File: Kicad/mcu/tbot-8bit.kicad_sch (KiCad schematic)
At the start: 6 parts

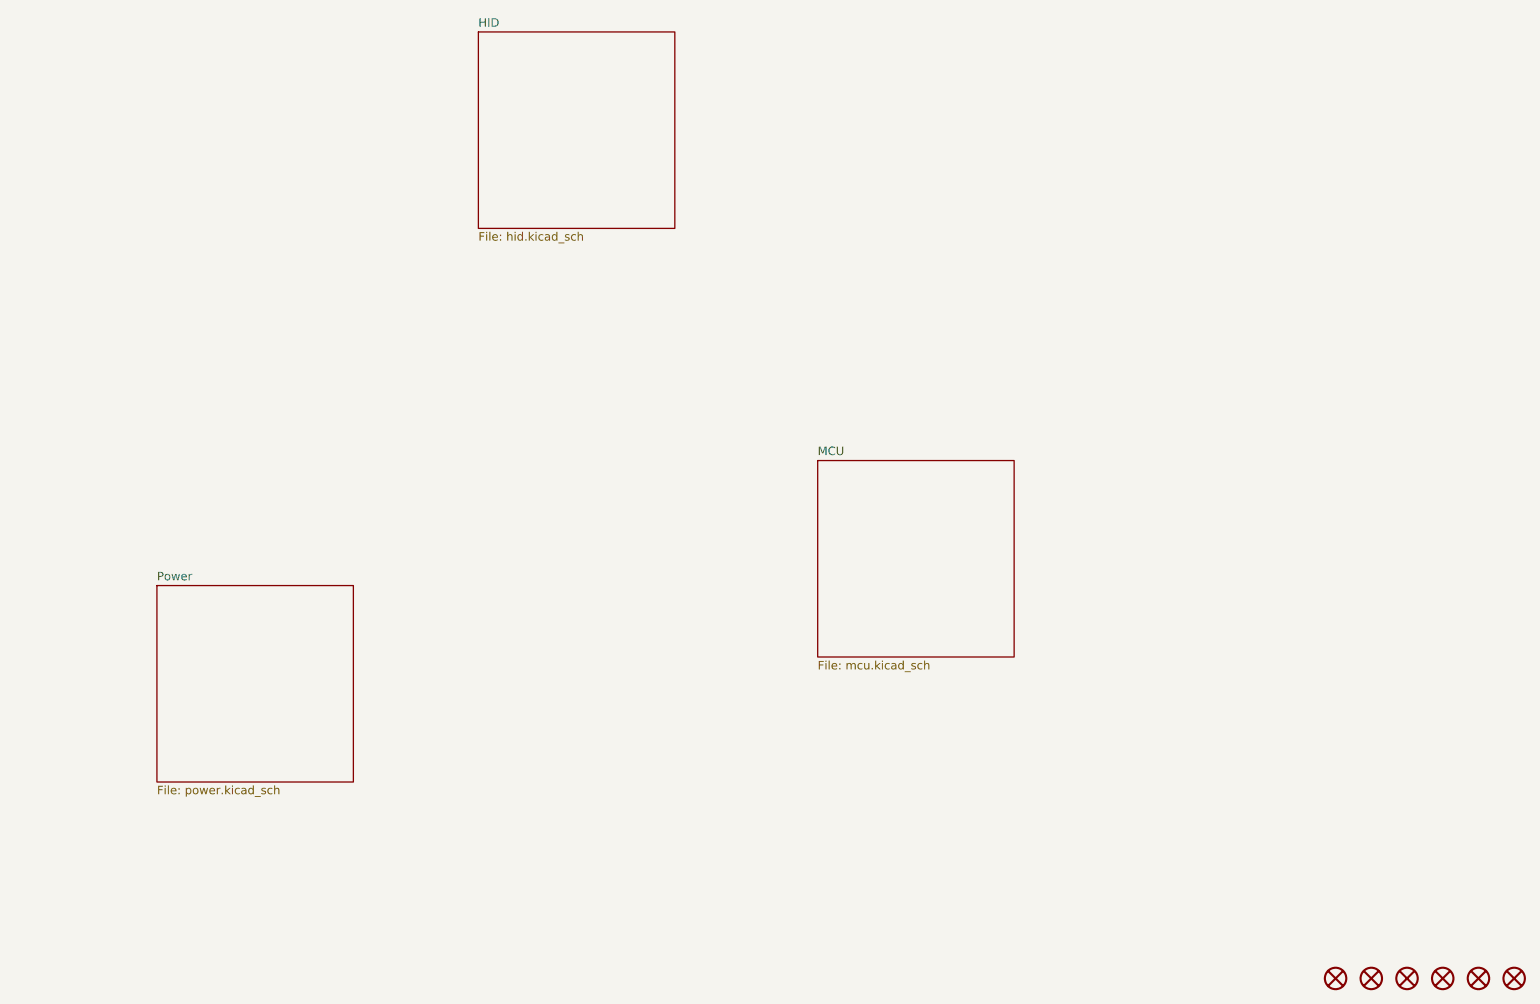
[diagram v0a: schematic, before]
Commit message: Update MCU 8Bit
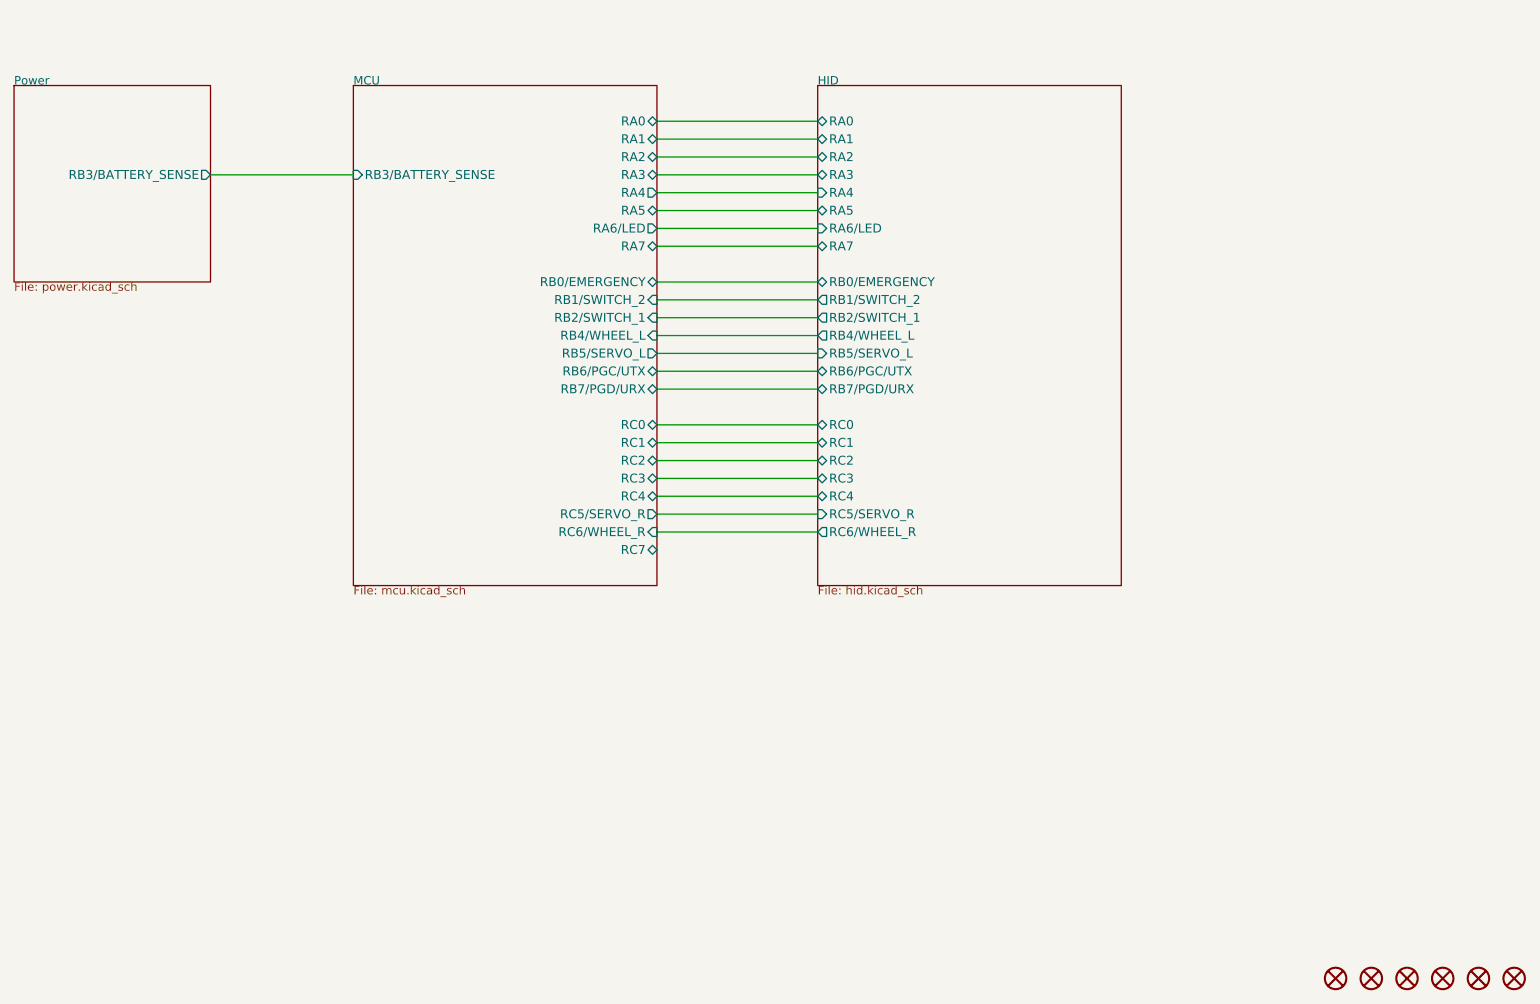
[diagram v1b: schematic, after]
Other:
- sheet HID ports: added RA0, RA1, RA2, RA3, RA4, RA5, RA6/LED, RA7, RB0/EMERGENCY, RB1/SWITCH_2, RB2/SWITCH_1, RB4/WHEEL_L, RB5/SERVO_L, RB6/PGC/UTX, RB7/PGD/URX, RC0, RC1, RC2, RC3, RC4, RC5/SERVO_R, RC6/WHEEL_R; removed none
- sheet MCU ports: added RA0, RA1, RA2, RA3, RA4, RA5, RA6/LED, RA7, RB0/EMERGENCY, RB1/SWITCH_2, RB2/SWITCH_1, RB3/BATTERY_SENSE, RB4/WHEEL_L, RB5/SERVO_L, RB6/PGC/UTX, RB7/PGD/URX, RC0, RC1, RC2, RC3, RC4, RC5/SERVO_R, RC6/WHEEL_R, RC7; removed none
- sheet Power ports: added RB3/BATTERY_SENSE; removed none

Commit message: Update MCU
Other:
- sheet HID ports: added none; removed RA7, RB1/SWITCH_2, RB2/SWITCH_1, RC3, RC4
- sheet MCU ports: added none; removed RA7, RB1/SWITCH_2, RB2/SWITCH_1, RC3, RC4, RC7

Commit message: Update MCU
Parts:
- added H107, H108: MOUNTING-HOLE-3MM, tronixio:M3, symbol tronixio:MOUNTING-HOLE-3MM
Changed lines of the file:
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@@
     (stroke (width 0) (type default) (color 0 0 0 0))
-  )
-  (symbol (lib_id "tronixio:MOUNTING-HOLE-MASK-3MM") (at 279.4 172.72 0) (unit 1)
-    (in_bom yes) (on_board yes)
-    (property "Reference" "H106" (id 0) (at 279.4 167.64 0)
-      (effects (font (size 1 1)) hide)
-    )
-    (property "Value" "MOUNTING-HOLE-MASK-3MM" (id 1) (at 279.4 170.18 0)
-      (effects (font (size 1 1)) hide)
-    )
-    (property "Footprint" "tronixio:M3-MASK" (id 2) (at 279.4 175.26 0)
-      (effects (font (size 1 1)) hide)
-    )
-    (property "Datasheet" "" (id 3) (at 279.4 172.72 0)
-      (effects (font (size 1 1)) hide)
-    )
-  )
-  (symbol (lib_id "tronixio:MOUNTING-HOLE-MASK-3MM") (at 274.32 172.72 0) (unit 1)
-    (in_bom yes) (on_board yes)
-    (property "Reference" "H105" (id 0) (at 274.32 167.64 0)
-      (effects (font (size 1 1)) hide)
-    )
-    (property "Value" "MOUNTING-HOLE-MASK-3MM" (id 1) (at 274.32 170.18 0)
-      (effects (font (size 1 1)) hide)
-    )
-    (property "Footprint" "tronixio:M3-MASK" (id 2) (at 274.32 175.26 0)
-      (effects (font (size 1 1)) hide)
-    )
-    (property "Datasheet" "" (id 3) (at 274.32 172.72 0)
-      (effects (font (size 1 1)) hide)
-    )
-  )
-  (symbol (lib_id "tronixio:MOUNTING-HOLE-MASK-3MM") (at 269.24 172.72 0) (unit 1)
-    (in_bom yes) (on_board yes)
-    (property "Reference" "H104" (id 0) (at 269.24 167.64 0)
-      (effects (font (size 1 1)) hide)
-    )
-    (property "Value" "MOUNTING-HOLE-MASK-3MM" (id 1) (at 269.24 170.18 0)
-      (effects (font (size 1 1)) hide)
-    )
-    (property "Footprint" "tronixio:M3-MASK" (id 2) (at 269.24 175.26 0)
-      (effects (font (size 1 1)) hide)
-    )
-    (property "Datasheet" "" (id 3) (at 269.24 172.72 0)
-      (effects (font (size 1 1)) hide)
-    )
   )
   (symbol (lib_id "tronixio:MOUNTING-HOLE-MASK-3MM") (at 264.16 172.72 0) (unit 1)
     (in_bom yes) (on_board yes)
-    (property "Reference" "H103" (id 0) (at 264.16 167.64 0)
+    (property "Reference" "H106" (id 0) (at 264.16 167.64 0)
       (effects (font (size 1 1)) hide)
     )
@@
     )
     (property "Datasheet" "" (id 3) (at 264.16 172.72 0)
+      (effects (font (size 1 1)) hide)
+    )
+  )
+  (symbol (lib_id "tronixio:MOUNTING-HOLE-MASK-3MM") (at 259.08 172.72 0) (unit 1)
+    (in_bom yes) (on_board yes)
+    (property "Reference" "H105" (id 0) (at 259.08 167.64 0)
+      (effects (font (size 1 1)) hide)
+    )
+    (property "Value" "MOUNTING-HOLE-MASK-3MM" (id 1) (at 259.08 170.18 0)
+      (effects (font (size 1 1)) hide)
+    )
+    (property "Footprint" "tronixio:M3-MASK" (id 2) (at 259.08 175.26 0)
+      (effects (font (size 1 1)) hide)
+    )
+    (property "Datasheet" "" (id 3) (at 259.08 172.72 0)
       (effects (font (size 1 1)) hide)
     )
@@
   (symbol (lib_id "tronixio:MOUNTING-HOLE-MASK-3MM") (at 254 172.72 0) (unit 1)
     (in_bom yes) (on_board yes)
-    (property "Reference" "H101" (id 0) (at 254 167.64 0)
+    (property "Reference" "H104" (id 0) (at 254 167.64 0)
       (effects (font (size 1 1)) hide)
     )
@@
     )
   )
-  (symbol (lib_id "tronixio:MOUNTING-HOLE-MASK-3MM") (at 259.08 172.72 0) (unit 1)
+  (symbol (lib_id "tronixio:MOUNTING-HOLE-3MM") (at 276.86 172.72 0) (unit 1)
+    (in_bom yes) (on_board yes) (fields_autoplaced)
+    (property "Reference" "H108" (id 0) (at 276.86 170.18 0)
+      (effects (font (size 1 1)) hide)
+    )
+    (property "Value" "MOUNTING-HOLE-3MM" (id 1) (at 276.86 175.26 0)
+      (effects (font (size 1 1)) hide)
+    )
+    (property "Footprint" "tronixio:M3" (id 2) (at 276.86 177.8 0)
+      (effects (font (size 1 1)) hide)
+    )
+    (property "Datasheet" "" (id 3) (at 276.86 180.34 0)
+      (effects (font (size 1 1)) hide)
+    )
+  )
+  (symbol (lib_id "tronixio:MOUNTING-HOLE-MASK-3MM") (at 248.92 172.72 0) (unit 1)
     (in_bom yes) (on_board yes)
-    (property "Reference" "H102" (id 0) (at 259.08 167.64 0)
-      (effects (font (size 1 1)) hide)
-    )
-    (property "Value" "MOUNTING-HOLE-MASK-3MM" (id 1) (at 259.08 170.18 0)
-      (effects (font (size 1 1)) hide)
-    )
-    (property "Footprint" "tronixio:M3-MASK" (id 2) (at 259.08 175.26 0)
-      (effects (font (size 1 1)) hide)
-    )
-    (property "Datasheet" "" (id 3) (at 259.08 172.72 0)
+    (property "Reference" "H103" (id 0) (at 248.92 167.64 0)
+      (effects (font (size 1 1)) hide)
+    )
+    (property "Value" "MOUNTING-HOLE-MASK-3MM" (id 1) (at 248.92 170.18 0)
+      (effects (font (size 1 1)) hide)
+    )
+    (property "Footprint" "tronixio:M3-MASK" (id 2) (at 248.92 175.26 0)
+      (effects (font (size 1 1)) hide)
+    )
+    (property "Datasheet" "" (id 3) (at 248.92 172.72 0)
+      (effects (font (size 1 1)) hide)
+    )
+  )
+  (symbol (lib_id "tronixio:MOUNTING-HOLE-3MM") (at 271.78 172.72 0) (unit 1)
+    (in_bom yes) (on_board yes) (fields_autoplaced)
+    (property "Reference" "H107" (id 0) (at 271.78 170.18 0)
+      (effects (font (size 1 1)) hide)
+    )
+    (property "Value" "MOUNTING-HOLE-3MM" (id 1) (at 271.78 175.26 0)
+      (effects (font (size 1 1)) hide)
+    )
+    (property "Footprint" "tronixio:M3" (id 2) (at 271.78 177.8 0)
+      (effects (font (size 1 1)) hide)
+    )
+    (property "Datasheet" "" (id 3) (at 271.78 180.34 0)
+      (effects (font (size 1 1)) hide)
+    )
+  )
+  (symbol (lib_id "tronixio:MOUNTING-HOLE-MASK-3MM") (at 238.76 172.72 0) (unit 1)
+    (in_bom yes) (on_board yes)
+    (property "Reference" "H101" (id 0) (at 238.76 167.64 0)
+      (effects (font (size 1 1)) hide)
+    )
+    (property "Value" "MOUNTING-HOLE-MASK-3MM" (id 1) (at 238.76 170.18 0)
+      (effects (font (size 1 1)) hide)
+    )
+    (property "Footprint" "tronixio:M3-MASK" (id 2) (at 238.76 175.26 0)
+      (effects (font (size 1 1)) hide)
+    )
+    (property "Datasheet" "" (id 3) (at 238.76 172.72 0)
+      (effects (font (size 1 1)) hide)
+    )
+  )
+  (symbol (lib_id "tronixio:MOUNTING-HOLE-MASK-3MM") (at 243.84 172.72 0) (unit 1)
+    (in_bom yes) (on_board yes)
+    (property "Reference" "H102" (id 0) (at 243.84 167.64 0)
+      (effects (font (size 1 1)) hide)
+    )
+    (property "Value" "MOUNTING-HOLE-MASK-3MM" (id 1) (at 243.84 170.18 0)
+      (effects (font (size 1 1)) hide)
+    )
+    (property "Footprint" "tronixio:M3-MASK" (id 2) (at 243.84 175.26 0)
+      (effects (font (size 1 1)) hide)
+    )
+    (property "Datasheet" "" (id 3) (at 243.84 172.72 0)
       (effects (font (size 1 1)) hide)
     )
@@
       (reference "H106") (unit 1) (value "MOUNTING-HOLE-MASK-3MM") (footprint "tronixio:M3-MASK")
     )
+    (path "/a1ff8905-9b82-47d7-be4a-eb2f2eb4d966"
+      (reference "H107") (unit 1) (value "MOUNTING-HOLE-3MM") (footprint "tronixio:M3")
+    )
+    (path "/63d48fd5-e5f1-41b9-bb53-8fbbf91dc3a7"
+      (reference "H108") (unit 1) (value "MOUNTING-HOLE-3MM") (footprint "tronixio:M3")
+    )
     (path "/6dca117b-1aaa-49ac-ac49-257b60ed2b71/132cd21e-ba37-4834-9ab5-84b40a7cc974"
